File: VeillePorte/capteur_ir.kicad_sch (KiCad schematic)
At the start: 5 parts, among them J23 CABLE MODULE VL53L4CD, Q1 BSS138

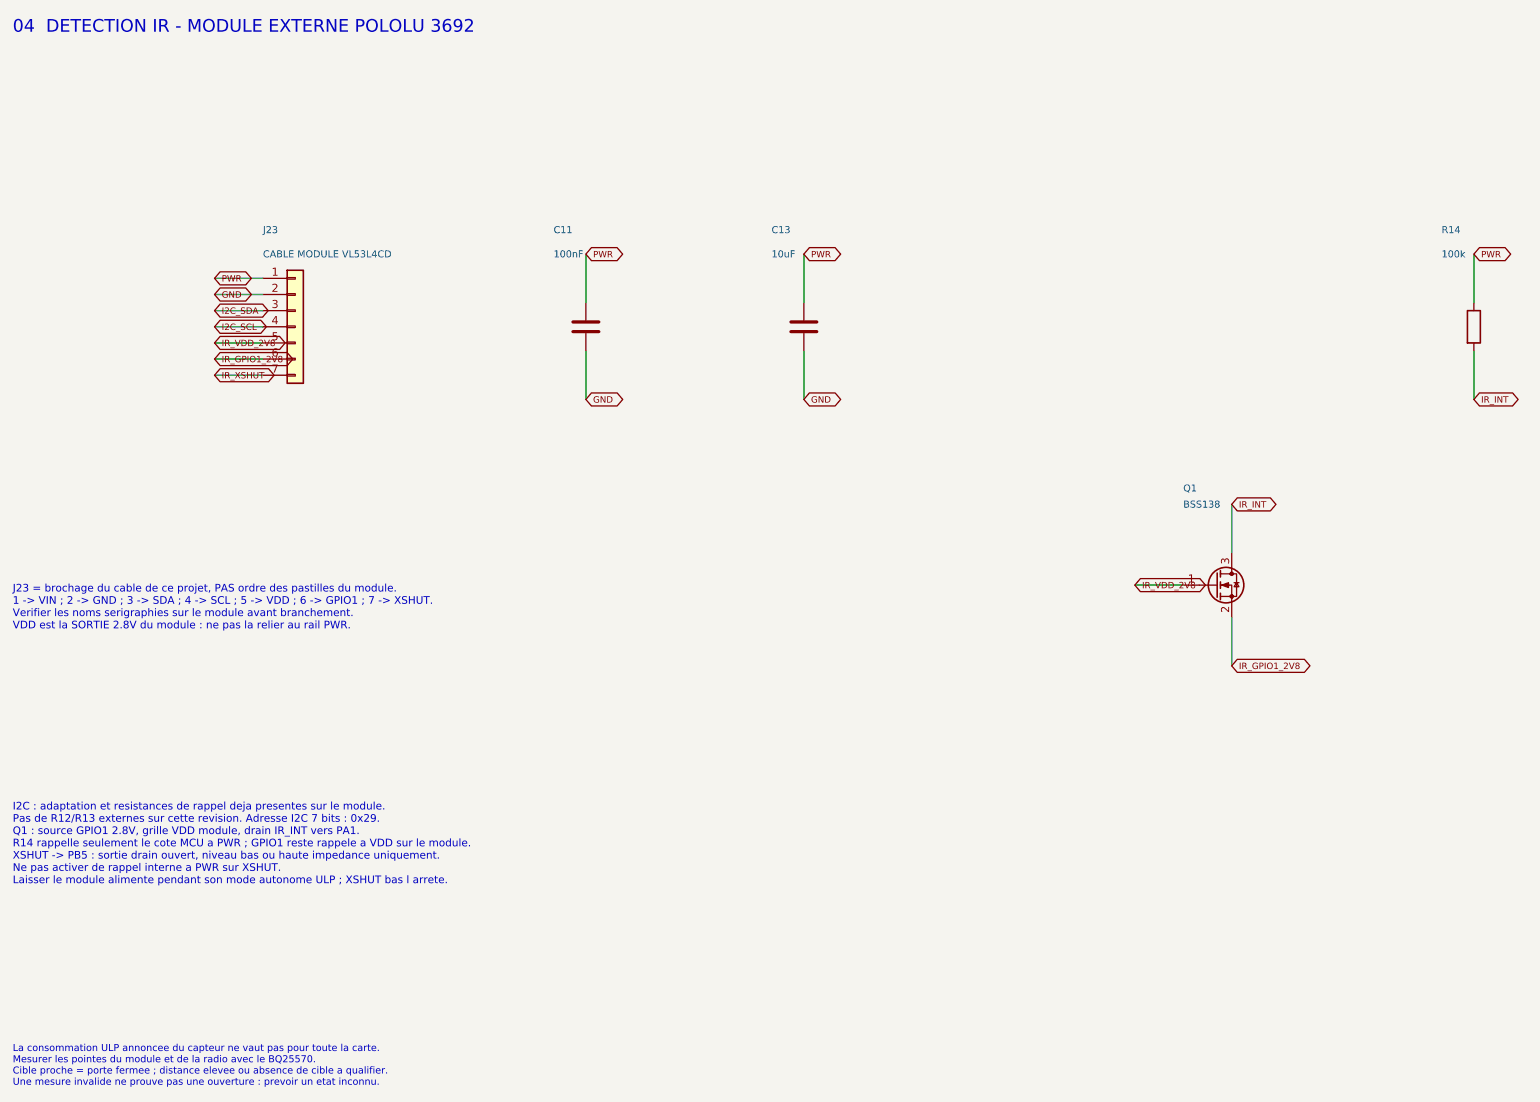
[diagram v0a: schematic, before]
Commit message: Regle le BQ25570 pour supercapacite 4V et structure la feuille RAK
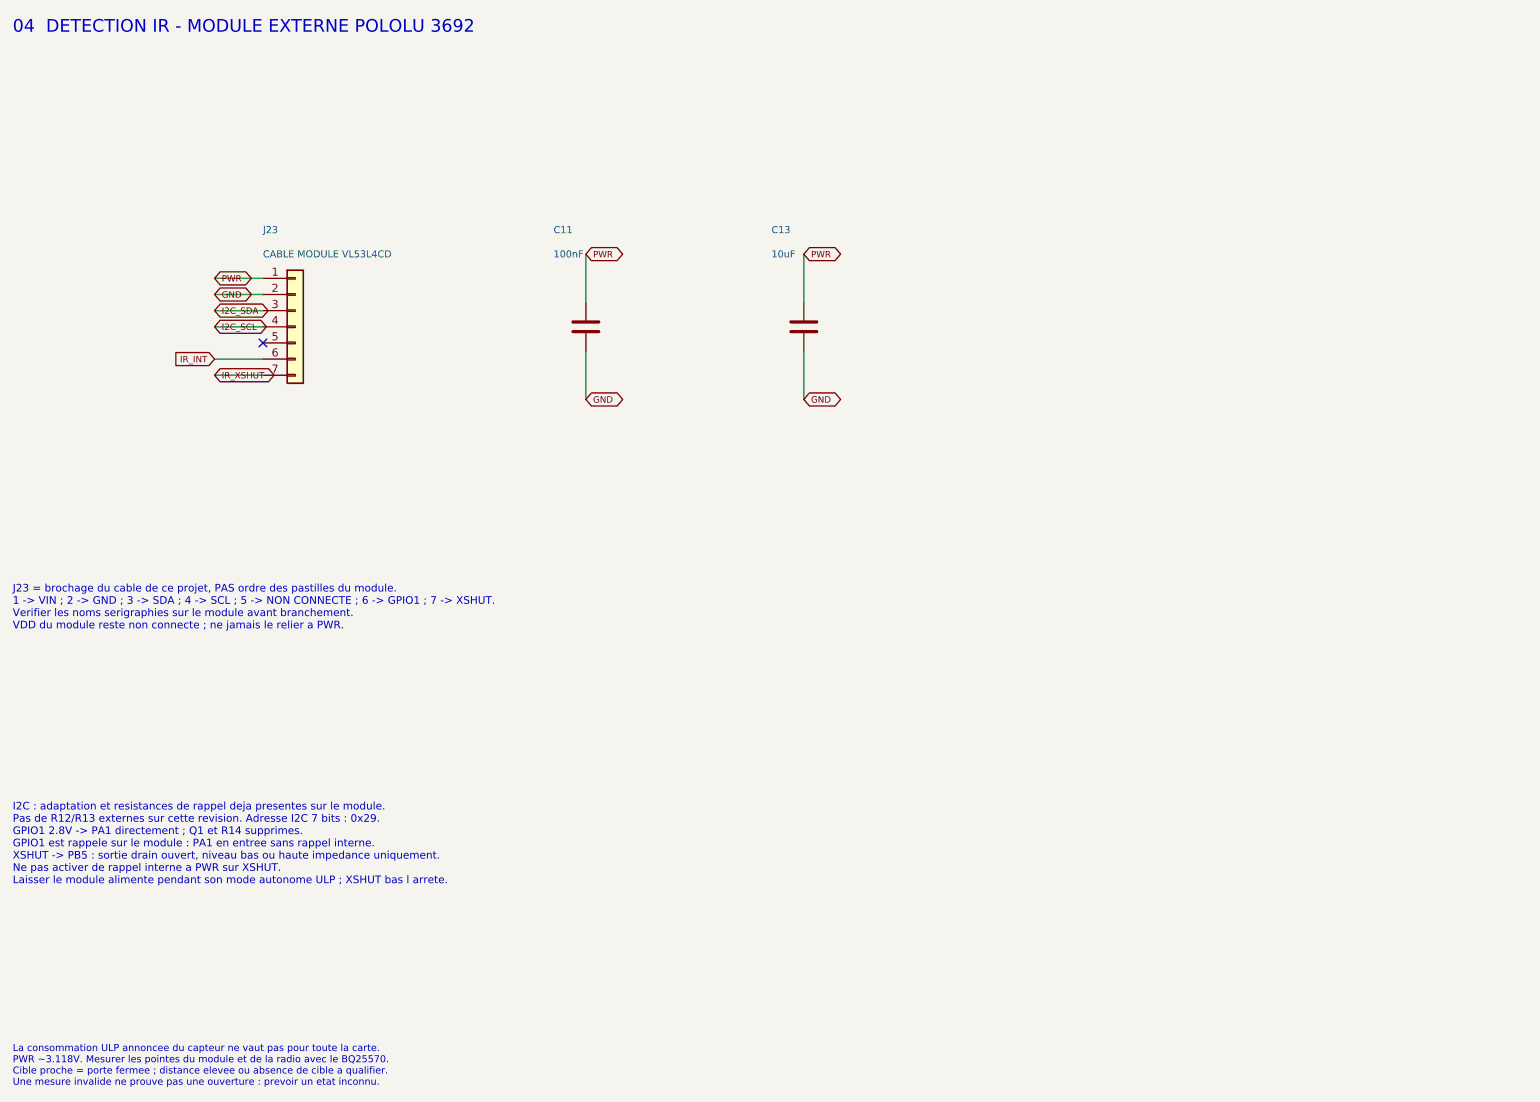
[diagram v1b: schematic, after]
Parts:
- removed Q1: BSS138, Package_TO_SOT_SMD:SOT-23, symbol Transistor_FET:BSS138
- removed R14: 100k, Resistor_SMD:R_0603_1608Metric, symbol Device:R
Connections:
- net IR_GPIO1_2V8 is gone; now on net IR_INT: J23.6 (Pin_6)
- net IR_VDD_2V8: no longer names the net of J23.5 (Pin_5)
- no-connect marks 0 -> 1
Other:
- note added: "I2C : adaptation et resistances de rappel deja presentes sur le module. Pas de R12/R13 externes sur cette revision. Adresse I2C 7 bits : 0x29. GPIO1 2.8V -> PA1 directement ; Q1 et R14 supprimes. GPIO1 est rappele sur le module : PA1 en entree sans rappel interne. XSHUT -> PB5 : sortie drain ouvert, niveau bas ou haute impedance uniquement. Ne pas activer de rappel interne a PWR sur XSHUT. Laisse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"
- note added: "J23 = brochage du cable de ce projet, PAS ordre des pastilles du module. 1 -> VIN ; 2 -> GND ; 3 -> SDA ; 4 -> SCL ; 5 -> NON CONNECTE ; 6 -> GPIO1 ; 7 -> XSHUT. Verifier les noms serigraphies sur le module avant branchement. VDD du module reste non connecte ; ne jamais le relier a PWR."
- note added: "La consommation ULP annoncee du capteur ne vaut pas pour toute la carte. PWR ~3.118V. Mesurer les pointes du module et de la radio avec le BQ25570. Cible proche = porte fermee ; distance elevee ou absence de cible a qualifier. Une mesure invalide ne prouve pas une ouverture : prevoir un etat inconnu."
- note removed: "I2C : adaptation et resistances de rappel deja presentes sur le module. Pas de R12/R13 externes sur cette revision. Adresse I2C 7 bits : 0x29. Q1 : source GPIO1 2.8V, grille VDD module, drain IR_INT vers PA1. R14 rappelle seulement le cote MCU a PWR ; GPIO1 reste rappele a VDD sur le module. XSHUT -> PB5 : sortie drain ouvert, niveau bas ou haute impedance uniquement. Ne pas activer de rappel int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"
- note removed: "J23 = brochage du cable de ce projet, PAS ordre des pastilles du module. 1 -> VIN ; 2 -> GND ; 3 -> SDA ; 4 -> SCL ; 5 -> VDD ; 6 -> GPIO1 ; 7 -> XSHUT. Verifier les noms serigraphies sur le module avant branchement. VDD est la SORTIE 2.8V du module : ne pas la relier au rail PWR."
- note removed: "La consommation ULP annoncee du capteur ne vaut pas pour toute la carte. Mesurer les pointes du module et de la radio avec le BQ25570. Cible proche = porte fermee ; distance elevee ou absence de cible a qualifier. Une mesure invalide ne prouve pas une ouverture : prevoir un etat inconnu."
